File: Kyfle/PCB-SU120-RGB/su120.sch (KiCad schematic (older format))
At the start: 229 parts, among them J1 MJ-4PP-9, J2 Conn_01x03, J3 Conn_01x08, J4 Conn_01x08, J5 Conn_01x03, J6 MJ-4PP-9, J7 Conn_02x05_Odd_Even, J8 Conn_02x05_Odd_Even, SW1 SW_PUSH_LED, SW10 SW_PUSH_LED, SW11 SW_PUSH_LED, SW12 SW_PUSH_LED, SW13 SW_PUSH_LED, SW14 SW_PUSH_LED, SW15 SW_PUSH_LED, SW16 SW_PUSH_LED, SW17 SW_PUSH_LED, SW18 SW_PUSH_LED, SW2 SW_PUSH_LED, SW20 Rotary_Encoder_Switch, SW21 Rotary_Encoder_Switch, SW22 SW_Push, SW3 SW_PUSH_LED, SW4 SW_PUSH_LED, SW5 SW_PUSH_LED, SW6 SW_PUSH_LED, SW7 SW_PUSH_LED, SW8 SW_PUSH_LED, SW9 SW_PUSH_LED, U1 ProMicro

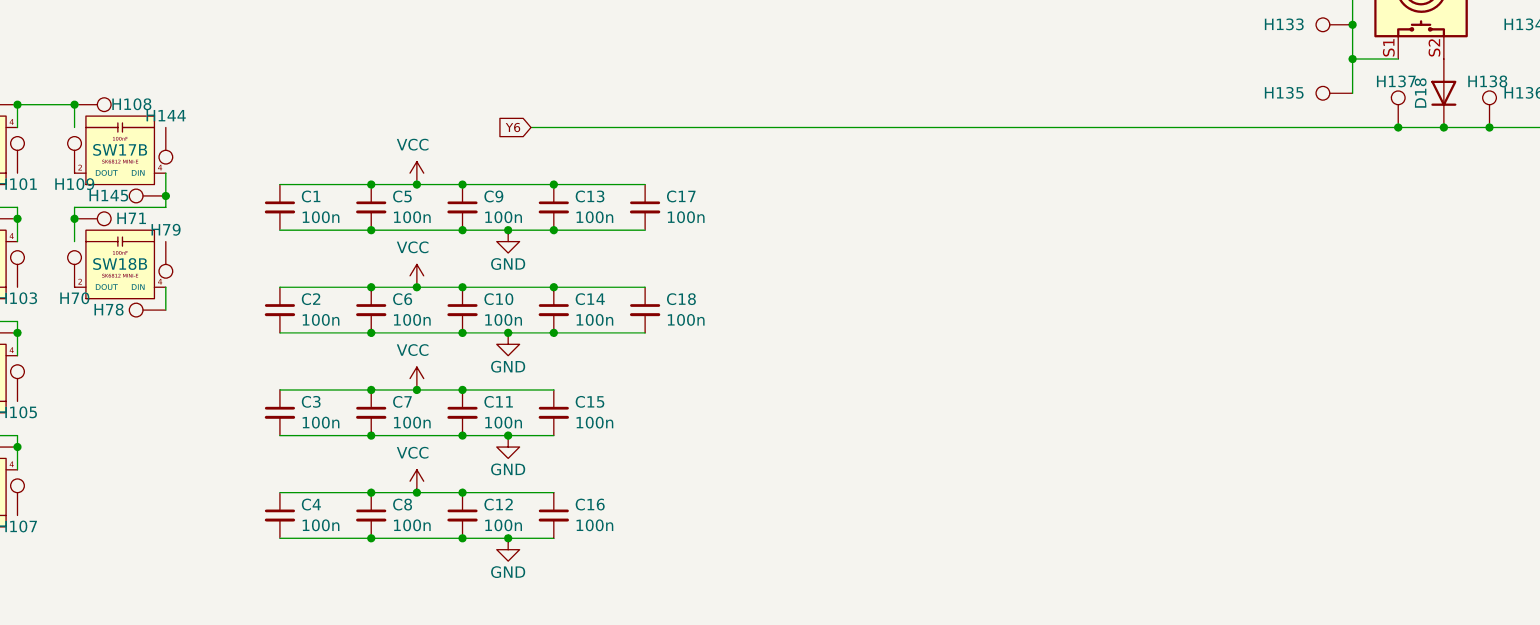
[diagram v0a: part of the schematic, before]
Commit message: Adding 4 RGB bit boards to the PCB
Replacing some of the spacers.
Based on SK6812 Mini-E.
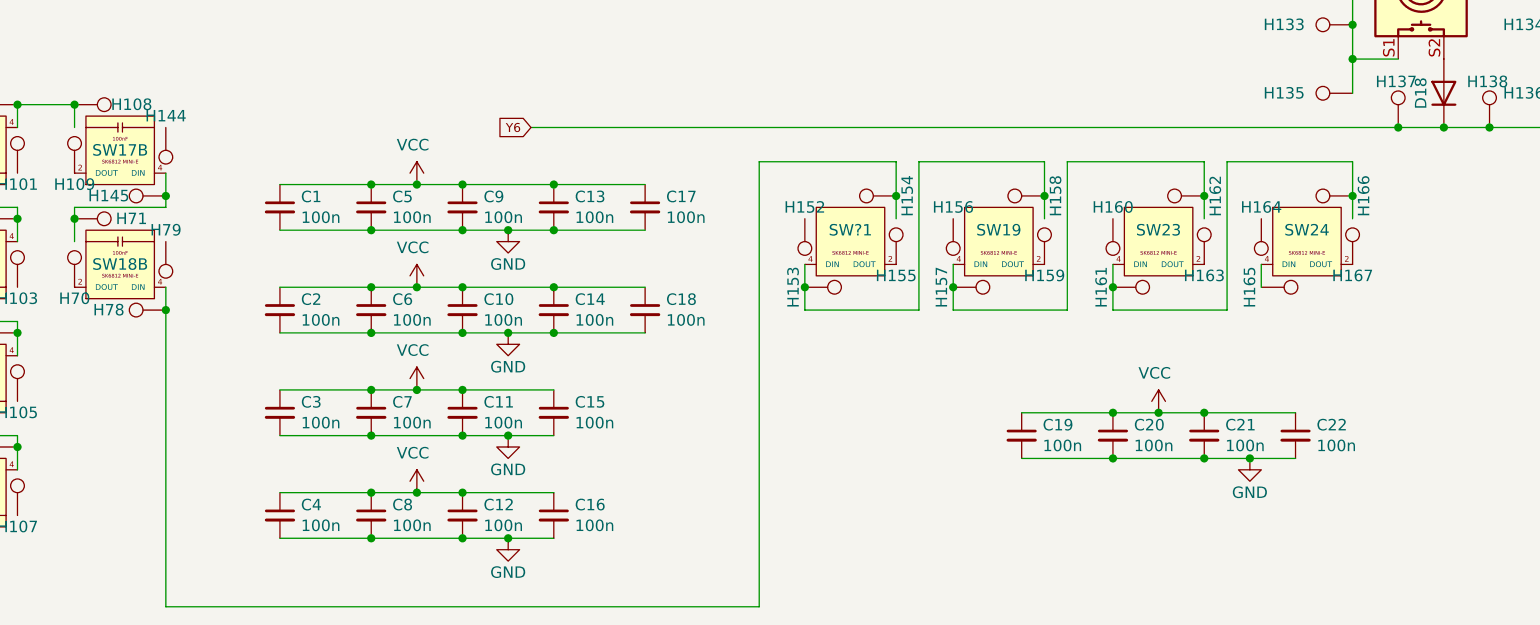
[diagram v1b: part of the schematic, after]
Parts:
- added C19, C20, C21, C22: 100n, Capacitor_SMD:C_0603_1608Metric_Pad1.08x0.95mm_HandSolder, symbol Device:C_Small
- added H152, H153, H154, H155, H156, H157, H158, H159, H160, H161, H162, H163, H164, H165, H166, H167: MountingHole_Pad, #footprint:1pin_conn, symbol Connector:TestPoint
- added SW19, SW23, SW24, SW?1: LED_SK6812_Mini_E, #footprint:SK6812_Mini_E, symbol Sofle:LED_SK6812_Mini_E
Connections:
- wire segments 337 -> 373

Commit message: Reorganising the pro micro bit board
- Changed how the jumper selectors work (the ones needed for reversible usage of the board)
- As it maded more space, I increased even more the power delivery for LED use case
- Changed footprint of OLED connector. Instead of just being through holes, they are now solderable through holes (though not connected to anything). It should help for mechanical stability of the screen.
- Small changes to hole sizes
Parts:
- removed J5: Conn_01x03, #footprint:StripLED_rev2, symbol Connector_Generic:Conn_01x03
- removed JP1, JP2, JP3, JP4, JP5, JP6: SolderJumper_2_Open, #footprint:SolderJumper-2_P1.3mm_Open_Pad1.0x1.0mm, symbol Jumper:SolderJumper_2_Open
- added JP101, JP102, JP103, JP104, JP105, JP106, JP107, JP108: SolderJumper_3_Open, #footprint:SolderJumper-3_P1.3mm_Open_TrianglePad1.0x1.5mm_duplex, symbol Jumper:SolderJumper_3_Open
- added R101: 50R, Resistor_SMD:R_0603_1608Metric_Pad0.98x0.95mm_HandSolder, symbol Device:R_Small
- J2: footprint #footprint:StripLED_rev2 -> Connector_PinHeader_2.54mm:PinHeader_1x03_P2.54mm_Vertical
- renumbered SW?1 to LED1, SW19 to LED2, SW23 to LED3, SW24 to LED4
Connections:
- net labels removed: dummyGND, dummyVCC, dummydata, dummyled, reset2
- wire segments 373 -> 366
- no-connect marks 16 -> 18
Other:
- moved on the sheet: C19, C20, C21, C22, H57

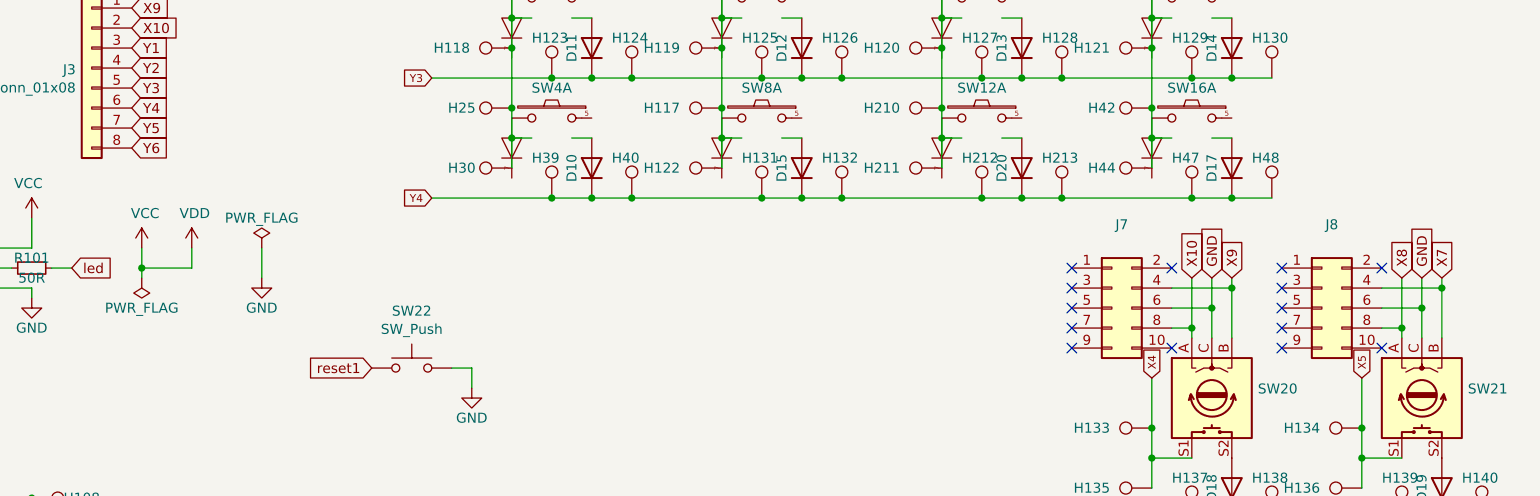
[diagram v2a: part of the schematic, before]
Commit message: Massive reduction in drill impacts and drill size diversity
It was suggested by a redittor that jlcpcb might charge engineering fees for too many holes.
So, all biscuits have been removed, all unused M1.4 holes have been removed, the signal pads (column, row, din, dout) have been converted from holes to just SMD pads as it should be fine if using enameled wire.
And the various holes have been harmonised to minimise number of drill sizes.

Also, number of vias have been greatly reduced, at the price of a bit less copper pour here and there (that's ok, if we cared about signal integrity we would you at least use a 4 layer stack up...).
The slots have been redone as footprints in order to control more easily their profile and achieve a consistent 1.2mm wide slot (including correct termination radius).

Finally, the Pro micro footprint has been switched to non-zigzag and rather use (tentative) a rivet-based socketing design.

All that came at the price of pretty much re-routing the entire board, again...
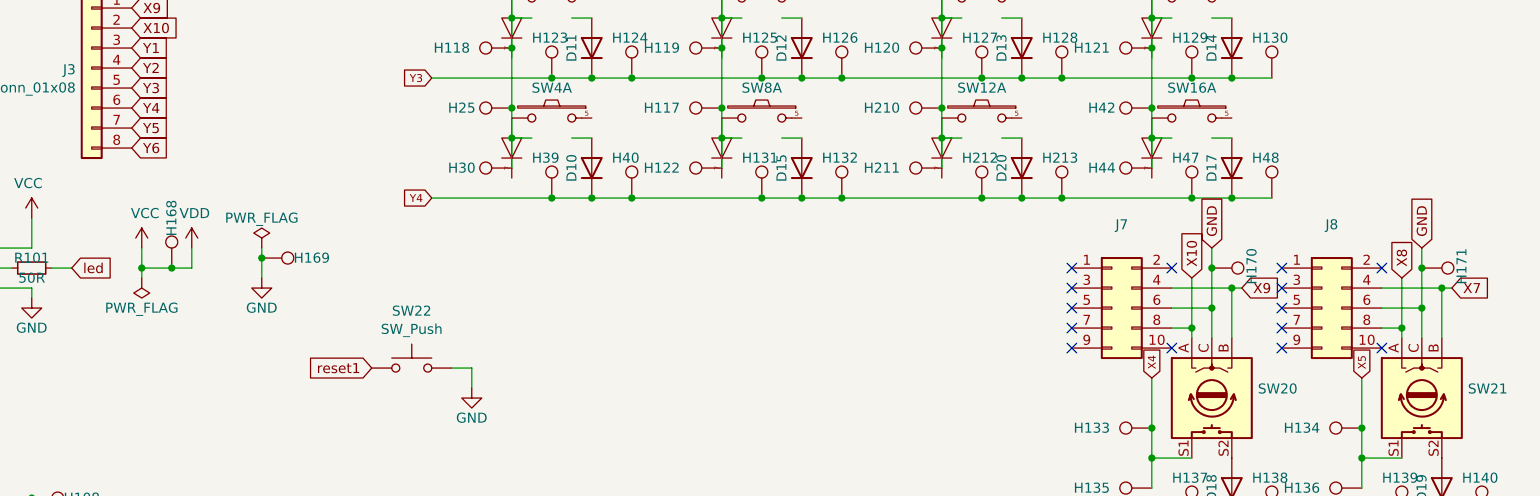
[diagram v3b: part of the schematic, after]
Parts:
- added H168, H169, H170, H171: MountingHole_Pad, #footprint:1pin_conn, symbol Connector:TestPoint
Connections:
- wire segments 366 -> 370
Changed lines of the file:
@@
 $EndComp
 Wire Wire Line
-	4750 4150 4750 4300
+	4750 4150 4750 4200
 Wire Wire Line
 	4150 4150 4150 4250
@@
 Wire Wire Line
 	10250 5200 10250 5350
-Text GLabel 9500 4300 1    50   Input ~ 0
+Text GLabel 9500 4150 1    50   Input ~ 0
 GND
-Text GLabel 10550 4300 1    50   Input ~ 0
+Text GLabel 10550 4150 1    50   Input ~ 0
 GND
 Text GLabel 9200 800  1    39   Input ~ 0
@@
 	9200 800  9200 1650
 Connection ~ 9200 1650
-Text GLabel 10650 4300 1    50   Input ~ 0
+Text GLabel 10700 4350 2    50   Input ~ 0
 X7
 Text GLabel 10450 4300 1    50   Input ~ 0
 X8
-Text GLabel 9600 4300 1    50   Input ~ 0
+Text GLabel 9650 4350 2    50   Input ~ 0
 X9
 Text GLabel 9400 4300 1    50   Input ~ 0
@@
 	9400 4300 9400 4550
 Wire Wire Line
-	9500 4300 9500 4450
-Wire Wire Line
-	9600 4300 9600 4350
+	9500 4150 9500 4250
 Wire Wire Line
 	10450 4300 10450 4550
 Wire Wire Line
-	10550 4300 10550 4450
-Wire Wire Line
-	10650 4300 10650 4350
+	10550 4150 10550 4250
 Wire Wire Line
 	9300 4350 9600 4350
-Connection ~ 9600 4350
 Wire Wire Line
 	9600 4350 9600 4600
@@
 $EndComp
 Wire Wire Line
-	4150 4250 4400 4250
+	4150 4250 4300 4250
 Wire Wire Line
 	4400 4250 4400 4150
@@
 Wire Wire Line
 	3500 4250 3400 4250
+Wire Wire Line
+	9650 4350 9600 4350
+Connection ~ 9600 4350
+Wire Wire Line
+	10700 4350 10650 4350
+$Comp
+L Connector:TestPoint H170
+U 1 1 617932EC
+P 9500 4250
+F 0 "H170" H 9400 4450 50  0000 L CNN
+F 1 "MountingHole_Pad" H 9600 4210 50  0001 L CNN
+F 2 "#footprint:1pin_conn" H 9500 4250 50  0001 C CNN
+F 3 "~" H 9500 4250 50  0001 C CNN
+	1    9500 4250
+	0    1    1    0
+$EndComp
+Connection ~ 9500 4250
+Wire Wire Line
+	9500 4250 9500 4450
+$Comp
+L Connector:TestPoint H171
+U 1 1 617E0E69
+P 10550 4250
+F 0 "H171" H 10450 4450 50  0000 L CNN
+F 1 "MountingHole_Pad" H 10650 4210 50  0001 L CNN
+F 2 "#footprint:1pin_conn" H 10550 4250 50  0001 C CNN
+F 3 "~" H 10550 4250 50  0001 C CNN
+	1    10550 4250
+	0    1    1    0
+$EndComp
+Connection ~ 10550 4250
+Wire Wire Line
+	10550 4250 10550 4450
+$Comp
+L Connector:TestPoint H168
+U 1 1 617E13D0
+P 4300 4250
+F 0 "H168" V 4300 4500 50  0000 C CNN
+F 1 "MountingHole_Pad" V 4446 4255 50  0001 C CNN
+F 2 "#footprint:1pin_conn" H 4300 4250 50  0001 C CNN
+F 3 "~" H 4300 4250 50  0001 C CNN
+	1    4300 4250
+	1    0    0    -1
+$EndComp
+Connection ~ 4300 4250
+Wire Wire Line
+	4300 4250 4400 4250
+$Comp
+L Connector:TestPoint H169
+U 1 1 617E23BC
+P 4750 4200
+F 0 "H169" V 4750 4450 50  0000 C CNN
+F 1 "MountingHole_Pad" V 4896 4205 50  0001 C CNN
+F 2 "#footprint:1pin_conn" H 4750 4200 50  0001 C CNN
+F 3 "~" H 4750 4200 50  0001 C CNN
+	1    4750 4200
+	0    1    1    0
+$EndComp
+Connection ~ 4750 4200
+Wire Wire Line
+	4750 4200 4750 4300
 $EndSCHEMATC

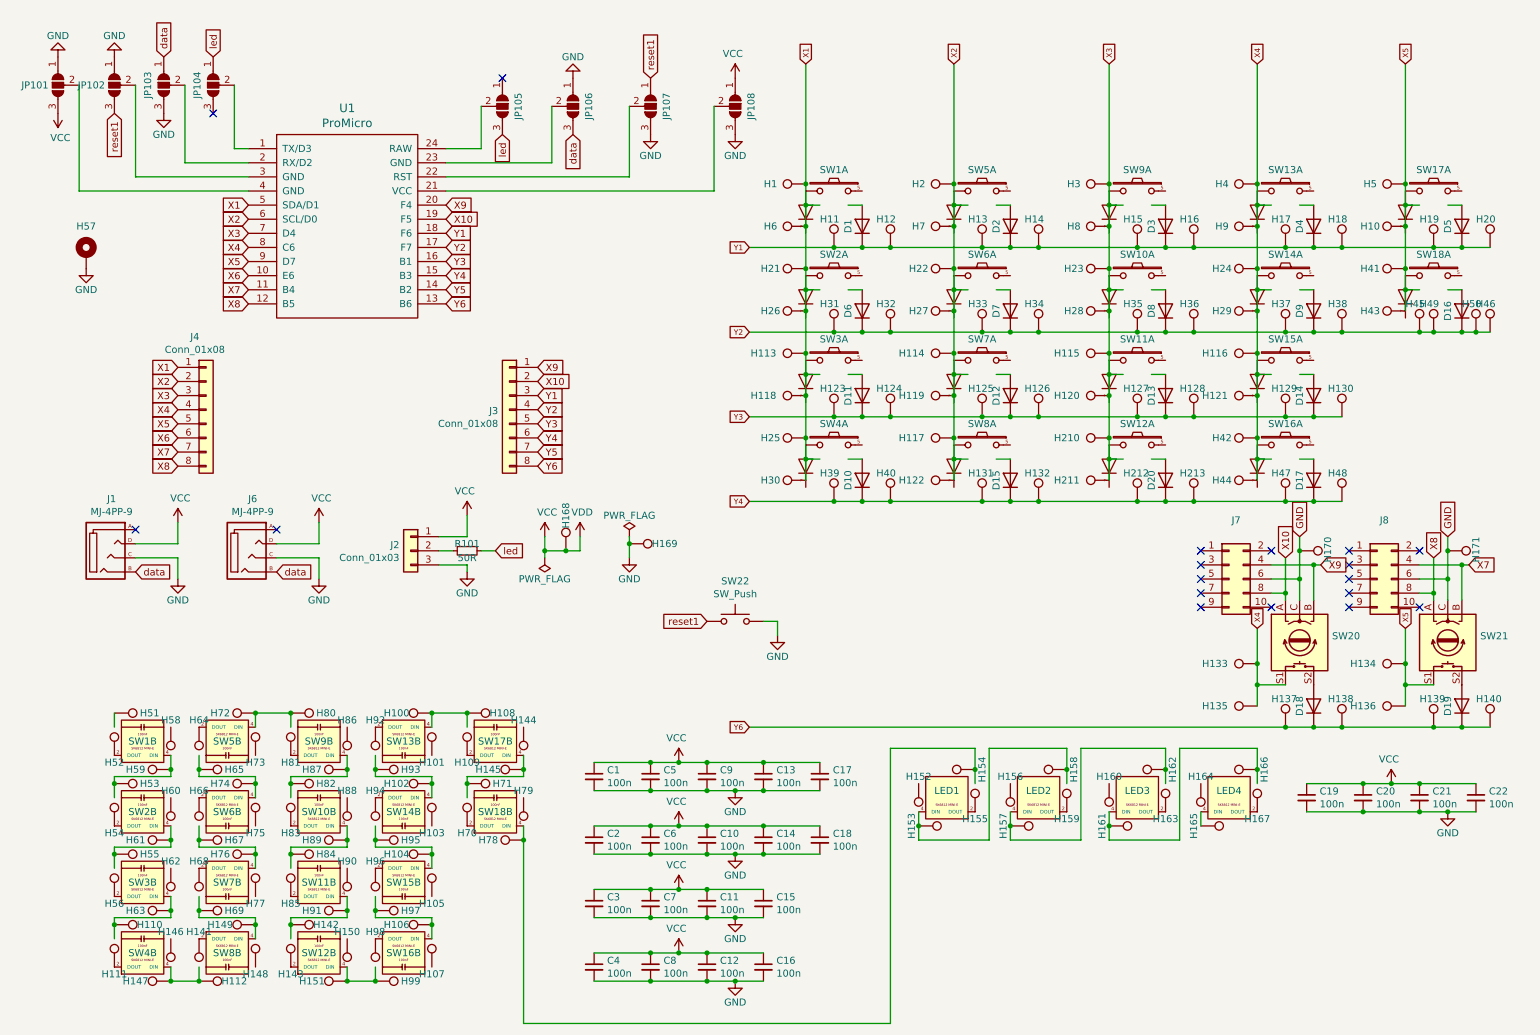
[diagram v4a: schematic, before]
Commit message: Massive redesign
- Realised the design was not reversible. Only solution was to mirror the two diagonal holes of each bit. But one of them was coliding with hotswap socket footprint. Until...
- I also realised that having the holes at these Y positions made the screw coming on top collide with the bottom of the switch housing...
- So switched to having two holes right in between each bit (vertically).
- Then I realised cheap pcb houses can have quite some limitations when it comes to exotic uses of slots. In particular, for jlcpcb:
  * They prefer tabs to be >= 4mm wide
  * They prefer at least 3mm of PCB next to a slot (ie. avoid slim inter-slots parts)
  * They prefer 0.4mm clearence from board edge when it is milled/routed
  * Watching some videos of their fab it seems they do the edge.cuts routing with a single 1mm bit. Ie. if you specify a larger radius they actually route it out. And if you specify a smaller radius (than 0.5mm) they cannot do it.

So, I redid the PCB. Twice... Again. For now...

I also started reorganising the projects. First part was to gather all footprints used accross the three boards. Makes cross-board editing of footprints easier.
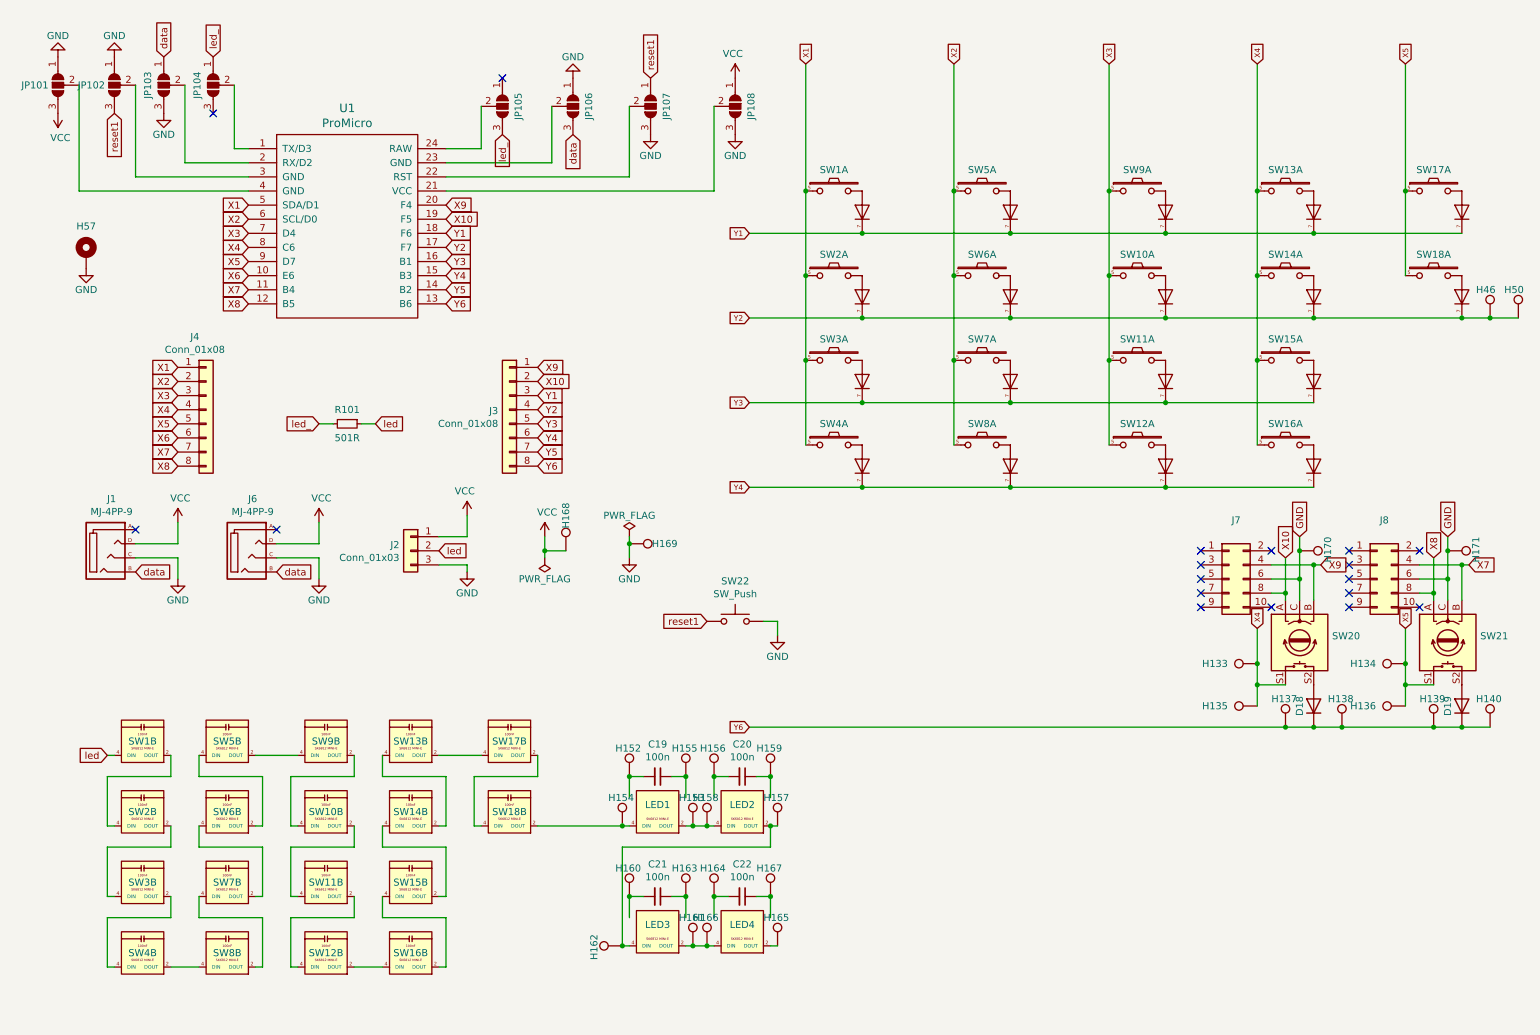
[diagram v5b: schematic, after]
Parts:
- removed C1, C10, C11, C12, C13, C14, C15, C16, C17, C18, C2, C3, C4, C5, C6, C7, C8, C9: 100n, Capacitor_SMD:C_0603_1608Metric_Pad1.08x0.95mm_HandSolder, symbol Device:C_Small
- removed D1, D10, D11, D12, D13, D14, D15, D16, D17, D2, D20, D3, D4, D5, D6, D7, D8, D9: D, #footprint:diode_TH_SMD_rev2, symbol Device:D
- removed H1, H10, H100, H101, H102, H103, H104, H105, H106, H107, H108, H109, H11, H110, H111, H112, H113, H114, H115, H116, H117, H118, H119, H12, H120, H121, H122, H123, H124, H125, H126, H127, H128, H129, H13, H130, H131, H132, H14, H141, H142, H143, H144, H145, H146, H147, H148, H149, H15, H150, H151, H16, H17, H18, H19, H2, H20, H21, H210, H211, H212, H213, H22, H23, H24, H25, H26, H27, H28, H29, H3, H30, H31, H32, H33, H34, H35, H36, H37, H38, H39, H4, H40, H41, H42, H43, H44, H45, H47, H48, H49, H5, H51, H52, H53, H54, H55, H56, H58, H59, H6, H60, H61, H62, H63, H64, H65, H66, H67, H68, H69, H7, H70, H71, H72, H73, H74, H75, H76, H77, H78, H79, H8, H80, H81, H82, H83, H84, H85, H86, H87, H88, H89, H9, H90, H91, H92, H93, H94, H95, H96, H97, H98, H99: MountingHole_Pad, #footprint:1pin_conn, symbol Connector:TestPoint
- C19, C20, C21, C22: footprint Capacitor_SMD:C_0603_1608Metric_Pad1.08x0.95mm_HandSolder -> #footprint:C_0603_0805_HandSolder
- H133, H134, H135, H136, H137, H138, H139, H140, H153, H154, H157, H158, H161, H162, H165, H166, H168, H169, H46, H50: footprint #footprint:1pin_conn -> #footprint:1pad_conn
- J2: footprint Connector_PinHeader_2.54mm:PinHeader_1x03_P2.54mm_Vertical -> #footprint:PinHeader_1x03_P2.54mm_Vertical
- R101: value 50R -> 501R
- SW1, SW10, SW11, SW12, SW13, SW14, SW15, SW16, SW17, SW18, SW2, SW3, SW4, SW5, SW6, SW7, SW8, SW9: footprint #footprint:CherryMX_MidHeight_RGB_Hotswap -> #footprint:CherryMX_MidHeight_RGB_Hotswap_v2
- U1: footprint #footprint:ArduinoProMicro-ZigZag_rev5 -> #footprint:ArduinoProMicro-Rivets
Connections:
- net labels added: led_
- net labels removed: VDD
- wire segments 370 -> 196
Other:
- moved on the sheet: H46, H50, LED1, LED2, LED3, LED4, R101, SW10A, SW11A, SW12A, SW13A, SW14A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
